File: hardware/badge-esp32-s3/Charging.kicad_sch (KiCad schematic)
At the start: 10 parts, among them J4 LiPo, Q3 HL2301A, U4 TP4056

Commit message: Moved Switch posistion
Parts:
- added SW9: SK-12F04-G050, lcsc-lib:SW-TH_G-SWITCH_SK-12F04-G050, symbol lcsc-lib:SK-12F04-G050
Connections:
- net GND: now also SW9.3
- net VOUT: now also SW9.2; no longer D10.1, Q3.2 (S)
- new net: D10.1, Q3.2 (S), SW9.1
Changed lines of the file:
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@@
+	)
+	(junction
+		(at 120.65 67.31)
+		(diameter 0)
+		(color 0 0 0 0)
 	)
 	(junction
@@
 	)
 	(junction
-		(at 120.65 67.31)
-		(diameter 0)
-		(color 0 0 0 0)
-	)
-	(junction
 		(at 106.68 58.42)
 		(diameter 0)
@@
 	(wire
 		(pts
-			(xy 120.65 67.31) (xy 120.65 63.5)
+			(xy 133.35 67.31) (xy 120.65 67.31)
 		)
 		(stroke
@@
 	(wire
 		(pts
-			(xy 120.65 73.66) (xy 120.65 67.31)
+			(xy 120.65 63.5) (xy 120.65 67.31)
 		)
 		(stroke
@@
 	(wire
 		(pts
-			(xy 143.51 67.31) (xy 120.65 67.31)
+			(xy 143.51 67.31) (xy 135.89 67.31)
+		)
+		(stroke
+			(width 0)
+			(type default)
+		)
+	)
+	(wire
+		(pts
+			(xy 133.35 63.5) (xy 133.35 67.31)
+		)
+		(stroke
+			(width 0)
+			(type default)
+		)
+	)
+	(wire
+		(pts
+			(xy 138.43 63.5) (xy 157.48 63.5)
+		)
+		(stroke
+			(width 0)
+			(type default)
+		)
+	)
+	(wire
+		(pts
+			(xy 120.65 67.31) (xy 120.65 73.66)
+		)
+		(stroke
+			(width 0)
+			(type default)
+		)
+	)
+	(wire
+		(pts
+			(xy 135.89 67.31) (xy 135.89 63.5)
 		)
 		(stroke
@@
 	)
 	(symbol
+		(lib_id "power:GND")
+		(at 157.48 63.5 90)
+		(unit 1)
+		(exclude_from_sim no)
+		(in_bom yes)
+		(on_board yes)
+		(dnp no)
+		(fields_autoplaced yes)
+		(property "Reference" "#PWR046"
+			(at 163.83 63.5 0)
+			(effects
+				(font
+					(size 1.27 1.27)
+				)
+				(hide yes)
+			)
+		)
+		(property "Value" "GND"
+			(at 161.29 63.4999 90)
+			(effects
+				(font
+					(size 1.27 1.27)
+				)
+				(justify right)
+			)
+		)
+		(property "Footprint" ""
+			(at 157.48 63.5 0)
+			(effects
+				(font
+					(size 1.27 1.27)
+				)
+				(hide yes)
+			)
+		)
+		(property "Datasheet" ""
+			(at 157.48 63.5 0)
+			(effects
+				(font
+					(size 1.27 1.27)
+				)
+				(hide yes)
+			)
+		)
+		(property "Description" "Power symbol creates a global label with name \"GND\" , ground"
+			(at 157.48 63.5 0)
+			(effects
+				(font
+					(size 1.27 1.27)
+				)
+				(hide yes)
+			)
+		)
+		(pin "1"
+		)
+		(instances
+			(project ""
+				(path "/e2af9a6c-dbe9-4de2-9ba6-ea213a7300ec/9131a646-b9dc-4004-a7df-1b58b7ca0b9a"
+					(reference "#PWR046")
+					(unit 1)
+				)
+			)
+		)
+	)
+	(symbol
 		(lib_id "PCM_JLCPCB-Capacitors:0603,10uF,(2)")
 		(at 106.68 87.63 0)
@@
 					(unit 1)
 				)
+			)
+		)
+	)
+	(symbol
+		(lib_id "lcsc-lib:SK-12F04-G050")
+		(at 135.89 58.42 0)
+		(unit 1)
+		(exclude_from_sim no)
+		(in_bom yes)
+		(on_board yes)
+		(dnp no)
+		(fields_autoplaced yes)
+		(property "Reference" "SW9"
+			(at 139.7 55.8799 0)
+			(effects
+				(font
+					(size 1.27 1.27)
+				)
+				(justify left)
+			)
+		)
+		(property "Value" "SK-12F04-G050"
+			(at 139.7 58.4199 0)
+			(effects
+				(font
+					(size 1.27 1.27)
+				)
+				(justify left)
+			)
+		)
+		(property "Footprint" "lcsc-lib:SW-TH_G-SWITCH_SK-12F04-G050"
+			(at 135.89 71.12 0)
+			(effects
+				(font
+					(size 1.27 1.27)
+				)
+				(hide yes)
+			)
+		)
+		(property "Datasheet" ""
+			(at 135.89 58.42 0)
+			(effects
+				(font
+					(size 1.27 1.27)
+				)
+				(hide yes)
+			)
+		)
+		(property "Description" ""
+			(at 135.89 58.42 0)
+			(effects
+				(font
+					(size 1.27 1.27)
+				)
+				(hide yes)
+			)
+		)
+		(property "LCSC Part" "C2848876"
+			(at 135.89 73.66 0)
+			(effects
+				(font
+					(size 1.27 1.27)
+				)
+				(hide yes)
+			)
+		)
+		(pin "2"
+		)
+		(pin "1"
+		)
+		(pin "3"
+		)
+		(instances
+			(project "badge-esp32-s3"
+				(path "/e2af9a6c-dbe9-4de2-9ba6-ea213a7300ec/9131a646-b9dc-4004-a7df-1b58b7ca0b9a"
+					(reference "SW9")
+					(unit 1)
+				)

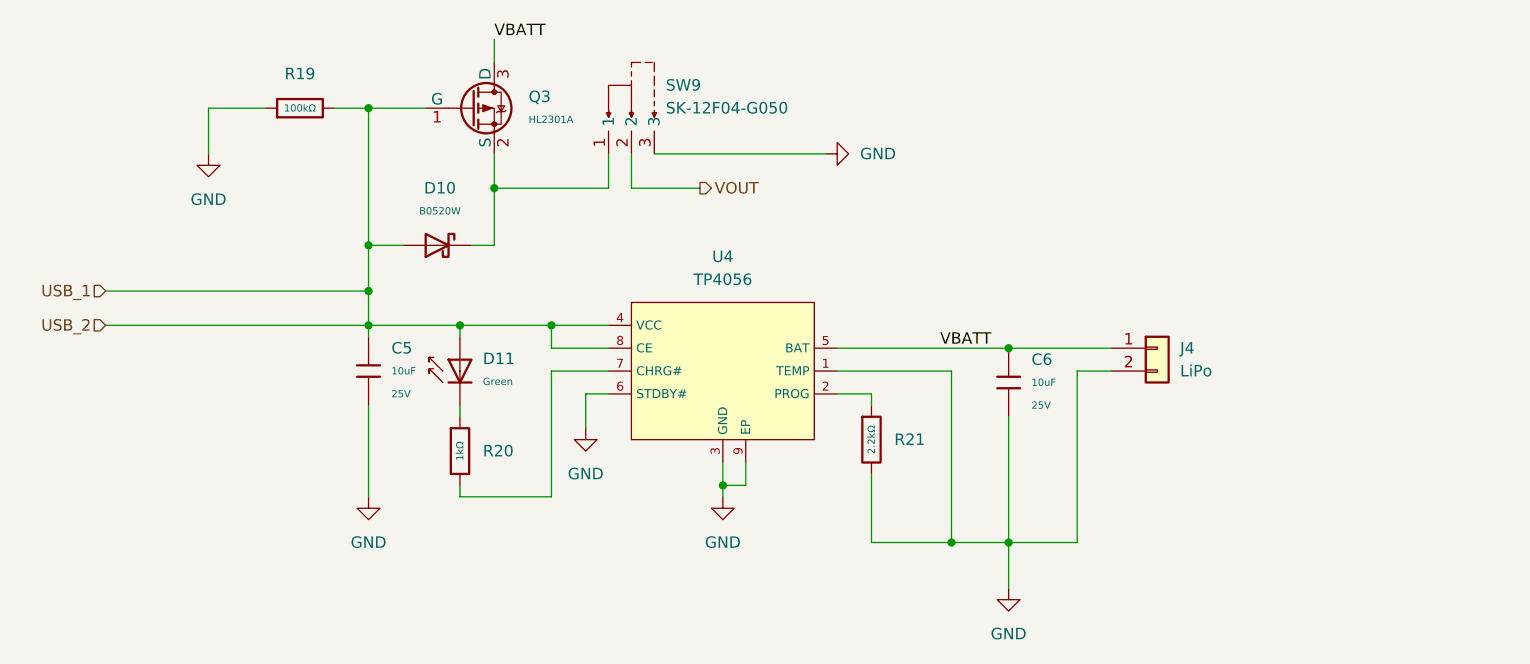
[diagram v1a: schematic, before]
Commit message: Fleshed out schematic with all exposed pins
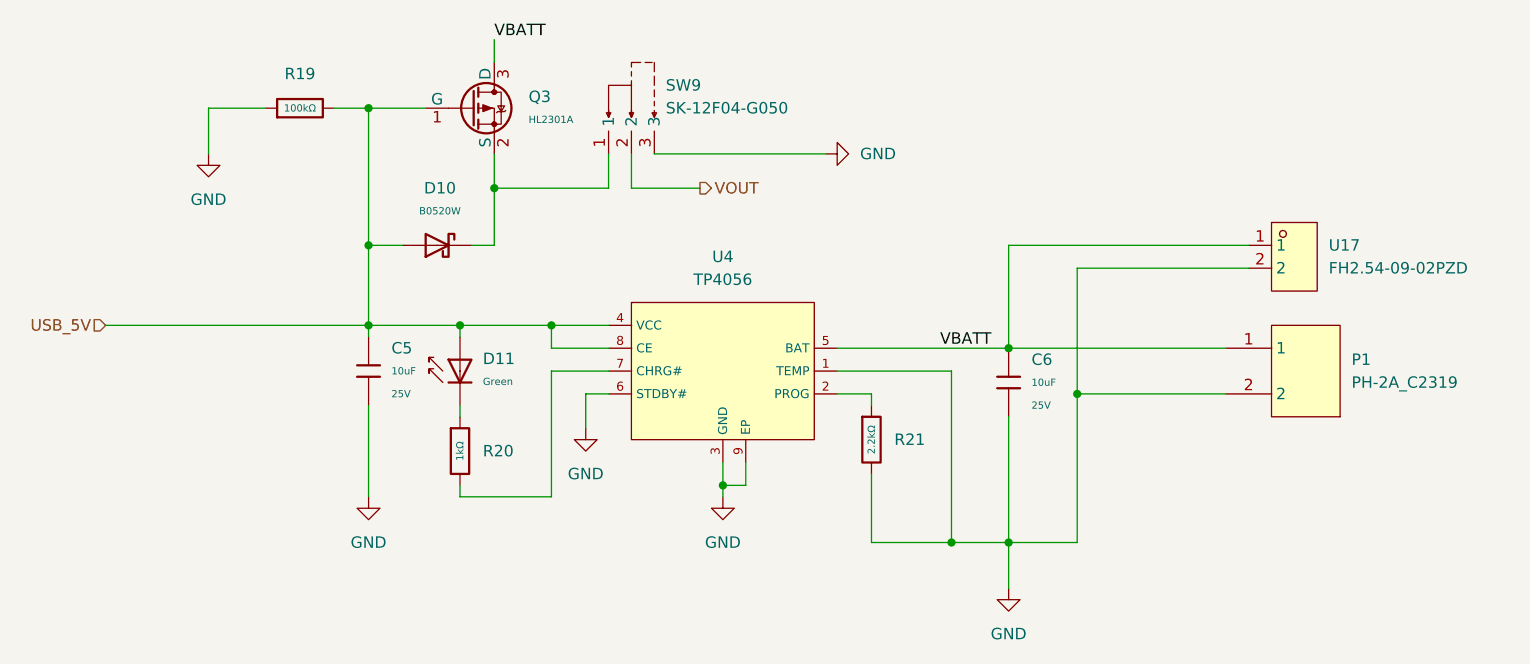
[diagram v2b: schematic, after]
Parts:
- removed J4: LiPo, Connector_JST:JST_PH_S2B-PH-K_1x02_P2.00mm_Horizontal, symbol Connector_Generic:Conn_01x02
- added P1: PH-2A_C2319, lcsc-lib:CONN-TH_2P-P2.00_PH-2A_C2319, symbol lcsc-lib:PH-2A_C2319
- added U17: FH2.54-09-02PZD, lcsc-lib:HDR-TH_2P-P2.54-V-M-5, symbol lcsc-lib:FH2.54-09-02PZD
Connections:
- net GND: now also P1.2, U17.2
- net VBATT: now also P1.1, U17.1
- net USB_1 renamed USB_5V
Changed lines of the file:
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@@
-	)
-	(junction
-		(at 106.68 78.74)
-		(diameter 0)
-		(color 0 0 0 0)
 	)
 	(junction
@@
 	)
 	(junction
+		(at 185.42 90.17)
+		(diameter 0)
+		(color 0 0 0 0)
+	)
+	(junction
 		(at 106.68 73.66)
 		(diameter 0)
@@
 	(wire
 		(pts
+			(xy 185.42 76.2) (xy 185.42 90.17)
+		)
+		(stroke
+			(width 0)
+			(type default)
+		)
+	)
+	(wire
+		(pts
 			(xy 118.11 73.66) (xy 120.65 73.66)
 		)
@@
 	(wire
 		(pts
-			(xy 189.23 87.63) (xy 185.42 87.63)
+			(xy 204.47 73.66) (xy 177.8 73.66)
+		)
+		(stroke
+			(width 0)
+			(type default)
+		)
+	)
+	(wire
+		(pts
+			(xy 185.42 90.17) (xy 201.93 90.17)
 		)
 		(stroke
@@
 	(wire
 		(pts
+			(xy 204.47 76.2) (xy 185.42 76.2)
+		)
+		(stroke
+			(width 0)
+			(type default)
+		)
+	)
+	(wire
+		(pts
 			(xy 162.56 106.68) (xy 171.45 106.68)
 		)
@@
 	(wire
 		(pts
+			(xy 177.8 73.66) (xy 177.8 85.09)
+		)
+		(stroke
+			(width 0)
+			(type default)
+		)
+	)
+	(wire
+		(pts
 			(xy 127 85.09) (xy 127 82.55)
 		)
@@
 	(wire
 		(pts
-			(xy 177.8 85.09) (xy 189.23 85.09)
+			(xy 177.8 85.09) (xy 201.93 85.09)
 		)
 		(stroke
@@
 	(wire
 		(pts
-			(xy 106.68 82.55) (xy 106.68 78.74)
+			(xy 106.68 73.66) (xy 106.68 82.55)
 		)
 		(stroke
@@
 	(wire
 		(pts
-			(xy 106.68 78.74) (xy 106.68 73.66)
-		)
-		(stroke
-			(width 0)
-			(type default)
-		)
-	)
-	(wire
-		(pts
 			(xy 95.25 58.42) (xy 88.9 58.42)
 		)
@@
 	(wire
 		(pts
-			(xy 77.47 78.74) (xy 106.68 78.74)
-		)
-		(stroke
-			(width 0)
-			(type default)
-		)
-	)
-	(wire
-		(pts
 			(xy 162.56 99.06) (xy 162.56 106.68)
 		)
@@
 	(wire
 		(pts
-			(xy 185.42 87.63) (xy 185.42 106.68)
+			(xy 185.42 90.17) (xy 185.42 106.68)
 		)
 		(stroke
@@
 		)
 	)
-	(hierarchical_label "USB_2"
+	(hierarchical_label "USB_5V"
 		(shape input)
 		(at 77.47 82.55 180)
-		(effects
-			(font
-				(size 1.27 1.27)
-			)
-			(justify right)
-		)
-	)
-	(hierarchical_label "USB_1"
-		(shape input)
-		(at 77.47 78.74 180)
 		(effects
 			(font
@@
 	)
 	(symbol
-		(lib_id "Connector_Generic:Conn_01x02")
-		(at 194.31 85.09 0)
-		(unit 1)
-		(exclude_from_sim no)
-		(in_bom yes)
-		(on_board yes)
-		(dnp no)
-		(fields_autoplaced yes)
-		(property "Reference" "J4"
-			(at 196.85 85.0899 0)
-			(effects
-				(font
-					(size 1.27 1.27)
-				)
-				(justify left)
-			)
-		)
-		(property "Value" "LiPo"
-			(at 196.85 87.6299 0)
-			(effects
-				(font
-					(size 1.27 1.27)
-				)
-				(justify left)
-			)
-		)
-		(property "Footprint" "Connector_JST:JST_PH_S2B-PH-K_1x02_P2.00mm_Horizontal"
-			(at 194.31 85.09 0)
-			(effects
-				(font
-					(size 1.27 1.27)
-				)
-				(hide yes)
-			)
-		)
-		(property "Datasheet" "~"
-			(at 194.31 85.09 0)
-			(effects
-				(font
-					(size 1.27 1.27)
-				)
-				(hide yes)
-			)
-		)
-		(property "Description" "Generic connector, single row, 01x02, script generated (kicad-library-utils/schlib/autogen/connector/)"
-			(at 194.31 85.09 0)
-			(effects
-				(font
-					(size 1.27 1.27)
-				)
-				(hide yes)
-			)
-		)
-		(pin "1"
-		)
-		(pin "2"
-		)
-		(instances
-			(project ""
-				(path "/e2af9a6c-dbe9-4de2-9ba6-ea213a7300ec/9131a646-b9dc-4004-a7df-1b58b7ca0b9a"
-					(reference "J4")
-					(unit 1)
-				)
-			)
-		)
-	)
-	(symbol
 		(lib_id "PCM_JLCPCB-Diodes:Schottky,B0520W")
 		(at 114.3 73.66 90)
@@
 					(unit 1)
 				)
+			)
+		)
+	)
+	(symbol
+		(lib_id "lcsc-lib:PH-2A_C2319")
+		(at 209.55 87.63 270)
+		(mirror x)
+		(unit 1)
+		(exclude_from_sim no)
+		(in_bom yes)
+		(on_board yes)
+		(dnp no)
+		(fields_autoplaced yes)
+		(property "Reference" "P1"
+			(at 215.9 86.3599 90)
+			(effects
+				(font
+					(size 1.27 1.27)
+				)
+				(justify left)
+			)
+		)
+		(property "Value" "PH-2A_C2319"
+			(at 215.9 88.8999 90)
+			(effects
+				(font
+					(size 1.27 1.27)
+				)
+				(justify left)
+			)
+		)
+		(property "Footprint" "lcsc-lib:CONN-TH_2P-P2.00_PH-2A_C2319"
+			(at 194.31 87.63 0)
+			(effects
+				(font
+					(size 1.27 1.27)
+				)
+				(hide yes)
+			)
+		)
+		(property "Datasheet" "https://lcsc.com/product-detail/PH-Connectors_PH-2A_C2319.html"
+			(at 191.77 87.63 0)
+			(effects
+				(font
+					(size 1.27 1.27)
+				)
+				(hide yes)
+			)
+		)
+		(property "Description" ""
+			(at 209.55 87.63 0)
+			(effects
+				(font
+					(size 1.27 1.27)
+				)
+				(hide yes)
+			)
+		)
+		(property "LCSC Part" "C2319"
+			(at 189.23 87.63 0)
+			(effects
+				(font
+					(size 1.27 1.27)
+				)
+				(hide yes)
+			)
+		)
+		(pin "1"
+		)
+		(pin "2"
+		)
+		(instances
+			(project ""
+				(path "/e2af9a6c-dbe9-4de2-9ba6-ea213a7300ec/9131a646-b9dc-4004-a7df-1b58b7ca0b9a"
+					(reference "P1")
+					(unit 1)
+				)
+			)
+		)
+	)
+	(symbol
+		(lib_id "lcsc-lib:FH2.54-09-02PZD")
+		(at 209.55 74.93 0)
+		(unit 1)
+		(exclude_from_sim no)
+		(in_bom yes)
+		(on_board yes)
+		(dnp no)
+		(fields_autoplaced yes)
+		(property "Reference" "U17"
+			(at 213.36 73.6599 0)
+			(effects
+				(font
+					(size 1.27 1.27)
+				)
+				(justify left)
+			)
+		)
+		(property "Value" "FH2.54-09-02PZD"
+			(at 213.36 76.1999 0)
+			(effects
+				(font
+					(size 1.27 1.27)
+				)
+				(justify left)
+			)
+		)
+		(property "Footprint" "lcsc-lib:HDR-TH_2P-P2.54-V-M-5"
+			(at 209.55 83.82 0)
+			(effects
+				(font
+					(size 1.27 1.27)
+				)
+				(hide yes)
+			)
+		)
+		(property "Datasheet" ""
+			(at 209.55 74.93 0)
+			(effects
+				(font
+					(size 1.27 1.27)
+				)
+				(hide yes)
+			)
+		)
+		(property "Description" ""
+			(at 209.55 74.93 0)
+			(effects
+				(font
+					(size 1.27 1.27)
+				)
+				(hide yes)
+			)
+		)
+		(property "LCSC Part" "C7500771"
+			(at 209.55 86.36 0)
+			(effects
+				(font
+					(size 1.27 1.27)
+				)
+				(hide yes)
+			)
+		)
+		(pin "2"
+		)
+		(pin "1"
+		)
+		(instances
+			(project ""
+				(path "/e2af9a6c-dbe9-4de2-9ba6-ea213a7300ec/9131a646-b9dc-4004-a7df-1b58b7ca0b9a"
+					(reference "U17")
+					(unit 1)
+				)

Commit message: Annotate schematic
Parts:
- renumbered C5 to C12, C6 to C13, D10 to D11, D11 to D12, R19 to R24, R20 to R25, R21 to R26, SW9 to SW3, U17 to U5
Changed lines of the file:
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@@
 		(dnp no)
 		(fields_autoplaced yes)
-		(property "Reference" "#PWR032"
+		(property "Reference" "#PWR038"
 			(at 146.05 107.95 0)
 			(effects
@@
 			(project ""
 				(path "/e2af9a6c-dbe9-4de2-9ba6-ea213a7300ec/9131a646-b9dc-4004-a7df-1b58b7ca0b9a"
-					(reference "#PWR032")
+					(reference "#PWR038")
 					(unit 1)
 				)
@@
 		(dnp no)
 		(fields_autoplaced yes)
-		(property "Reference" "R20"
+		(property "Reference" "R25"
 			(at 119.38 96.5199 0)
 			(effects
@@
 			(project ""
 				(path "/e2af9a6c-dbe9-4de2-9ba6-ea213a7300ec/9131a646-b9dc-4004-a7df-1b58b7ca0b9a"
-					(reference "R20")
+					(reference "R25")
 					(unit 1)
 				)
@@
 		(dnp no)
 		(fields_autoplaced yes)
-		(property "Reference" "#PWR031"
+		(property "Reference" "#PWR040"
 			(at 177.8 118.11 0)
 			(effects
@@
 			(project ""
 				(path "/e2af9a6c-dbe9-4de2-9ba6-ea213a7300ec/9131a646-b9dc-4004-a7df-1b58b7ca0b9a"
-					(reference "#PWR031")
+					(reference "#PWR040")
 					(unit 1)
 				)
@@
 		(dnp no)
 		(fields_autoplaced yes)
-		(property "Reference" "C6"
+		(property "Reference" "C13"
 			(at 180.34 86.3599 0)
 			(effects
@@
 			(project ""
 				(path "/e2af9a6c-dbe9-4de2-9ba6-ea213a7300ec/9131a646-b9dc-4004-a7df-1b58b7ca0b9a"
-					(reference "C6")
+					(reference "C13")
 					(unit 1)
 				)
@@
 		(dnp no)
 		(fields_autoplaced yes)
-		(property "Reference" "R21"
+		(property "Reference" "R26"
 			(at 165.1 95.2499 0)
 			(effects
@@
 			(project ""
 				(path "/e2af9a6c-dbe9-4de2-9ba6-ea213a7300ec/9131a646-b9dc-4004-a7df-1b58b7ca0b9a"
-					(reference "R21")
+					(reference "R26")
 					(unit 1)
 				)
@@
 		(dnp no)
 		(fields_autoplaced yes)
-		(property "Reference" "#PWR046"
+		(property "Reference" "#PWR039"
 			(at 163.83 63.5 0)
 			(effects
@@
 			(project ""
 				(path "/e2af9a6c-dbe9-4de2-9ba6-ea213a7300ec/9131a646-b9dc-4004-a7df-1b58b7ca0b9a"
-					(reference "#PWR046")
+					(reference "#PWR039")
 					(unit 1)
 				)
@@
 		(dnp no)
 		(fields_autoplaced yes)
-		(property "Reference" "C5"
+		(property "Reference" "C12"
 			(at 109.22 85.0899 0)
 			(effects
@@
 			(project ""
 				(path "/e2af9a6c-dbe9-4de2-9ba6-ea213a7300ec/9131a646-b9dc-4004-a7df-1b58b7ca0b9a"
-					(reference "C5")
+					(reference "C12")
 					(unit 1)
 				)
@@
 		(dnp no)
 		(fields_autoplaced yes)
-		(property "Reference" "#PWR034"
+		(property "Reference" "#PWR037"
 			(at 130.81 100.33 0)
 			(effects
@@
 			(project ""
 				(path "/e2af9a6c-dbe9-4de2-9ba6-ea213a7300ec/9131a646-b9dc-4004-a7df-1b58b7ca0b9a"
-					(reference "#PWR034")
+					(reference "#PWR037")
 					(unit 1)
 				)
@@
 		(dnp no)
 		(fields_autoplaced yes)
-		(property "Reference" "D10"
+		(property "Reference" "D11"
 			(at 114.6175 67.31 90)
 			(effects
@@
 			(project ""
 				(path "/e2af9a6c-dbe9-4de2-9ba6-ea213a7300ec/9131a646-b9dc-4004-a7df-1b58b7ca0b9a"
-					(reference "D10")
+					(reference "D11")
 					(unit 1)
 				)
@@
 		(dnp no)
 		(fields_autoplaced yes)
-		(property "Reference" "R19"
+		(property "Reference" "R24"
 			(at 99.06 54.61 90)
 			(effects
@@
 			(project ""
 				(path "/e2af9a6c-dbe9-4de2-9ba6-ea213a7300ec/9131a646-b9dc-4004-a7df-1b58b7ca0b9a"
-					(reference "R19")
+					(reference "R24")
 					(unit 1)
 				)
@@
 		(dnp no)
 		(fields_autoplaced yes)
-		(property "Reference" "D11"
+		(property "Reference" "D12"
 			(at 119.38 86.2646 0)
 			(effects
@@
 			(project ""
 				(path "/e2af9a6c-dbe9-4de2-9ba6-ea213a7300ec/9131a646-b9dc-4004-a7df-1b58b7ca0b9a"
-					(reference "D11")
+					(reference "D12")
 					(unit 1)
 				)
@@
 		(dnp no)
 		(fields_autoplaced yes)
-		(property "Reference" "#PWR033"
+		(property "Reference" "#PWR035"
 			(at 88.9 69.85 0)
 			(effects
@@
 			(project ""
 				(path "/e2af9a6c-dbe9-4de2-9ba6-ea213a7300ec/9131a646-b9dc-4004-a7df-1b58b7ca0b9a"
-					(reference "#PWR033")
+					(reference "#PWR035")
 					(unit 1)
 				)
@@
 		(dnp no)
 		(fields_autoplaced yes)
-		(property "Reference" "SW9"
+		(property "Reference" "SW3"
 			(at 139.7 55.8799 0)
 			(effects
@@
 			(project "badge-esp32-s3"
 				(path "/e2af9a6c-dbe9-4de2-9ba6-ea213a7300ec/9131a646-b9dc-4004-a7df-1b58b7ca0b9a"
-					(reference "SW9")
+					(reference "SW3")
 					(unit 1)
 				)
@@
 		(dnp no)
 		(fields_autoplaced yes)
-		(property "Reference" "U17"
+		(property "Reference" "U5"
 			(at 213.36 73.6599 0)
 			(effects
@@
 			(project ""
 				(path "/e2af9a6c-dbe9-4de2-9ba6-ea213a7300ec/9131a646-b9dc-4004-a7df-1b58b7ca0b9a"
-					(reference "U17")
+					(reference "U5")
 					(unit 1)
 				)
